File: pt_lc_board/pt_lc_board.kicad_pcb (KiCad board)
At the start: 2 copper layers, 152.4 x 140 mm, 29 parts, among them J1 DSUB1, J2 DSUB2, J3 DSUB3, J4 PCIE Socket, U1 HX711_Breakout, U10 PCF8575_Breakout, U2 HX711_Breakout, U3 HX711_Breakout, U5 HX711_Breakout, U6 HX711_Breakout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

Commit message: Mostly finished with board.
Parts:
- removed U10: PCF8575_Breakout, PCF8575_Breakout:PCF8575_Breakout
- added R10: 4.7k, Resistor_SMD:R_0603_1608Metric, F.Cu at (132.9, 136.3)
- added R11: 4.7k, Resistor_SMD:R_0603_1608Metric, F.Cu at (132.9, 131.0)
- added R9: 4.7k, Resistor_SMD:R_0603_1608Metric, F.Cu at (137.2, 133.6)
- added U7: PCF8575_Breakout, PCF8575_Breakout:PCF8575_Breakout, F.Cu at (64.2, 130.6)
- J4: value PCIE Socket -> PCIE Card Edge; footprint PCIE-LP-01-01-F-DV-A-TR:SAMTEC_PCIE-LP-01-01-F-DV-A-TR -> Connector_PCBEdge:BUS_PCIexpress_x1
- R1, R13, R17: footprint Resistor_SMD:R_1206_3216Metric -> Resistor_SMD:R_0603_1608Metric
- R12: renamed from R5; footprint Resistor_SMD:R_1206_3216Metric -> Resistor_SMD:R_0603_1608Metric
- R14: renamed from R6; footprint Resistor_SMD:R_1206_3216Metric -> Resistor_SMD:R_0603_1608Metric
- R15: renamed from R14; footprint Resistor_SMD:R_1206_3216Metric -> Resistor_SMD:R_0603_1608Metric
- R16: renamed from R15; footprint Resistor_SMD:R_1206_3216Metric -> Resistor_SMD:R_0603_1608Metric
- R18: renamed from R16; footprint Resistor_SMD:R_1206_3216Metric -> Resistor_SMD:R_0603_1608Metric
- R19: renamed from R18; footprint Resistor_SMD:R_1206_3216Metric -> Resistor_SMD:R_0603_1608Metric
- R2: renamed from R9; footprint Resistor_SMD:R_1206_3216Metric -> Resistor_SMD:R_0603_1608Metric
- R3: renamed from R2; footprint Resistor_SMD:R_1206_3216Metric -> Resistor_SMD:R_0603_1608Metric
- R4: renamed from R10; footprint Resistor_SMD:R_1206_3216Metric -> Resistor_SMD:R_0603_1608Metric
- R5: renamed from R3; footprint Resistor_SMD:R_1206_3216Metric -> Resistor_SMD:R_0603_1608Metric
- R6: renamed from R11; footprint Resistor_SMD:R_1206_3216Metric -> Resistor_SMD:R_0603_1608Metric
- R7: renamed from R4; footprint Resistor_SMD:R_1206_3216Metric -> Resistor_SMD:R_0603_1608Metric
- R8: renamed from R12; footprint Resistor_SMD:R_1206_3216Metric -> Resistor_SMD:R_0603_1608Metric
- moved J4 11.2 mm to (125.0, 144.9)
- moved J3 0.36 mm to (66.9, 10.6)
- moved J1 0.25 mm to (13.6, 10.6)
- moved R7 0.15 mm to (11.9, 93.1)
- moved R18 0.13 mm to (62.8, 19.4)
- moved R14 0.10 mm to (114.0, 55.3)
- moved J2 0.09 mm to (117.8, 10.6)
- renumbered U5 to U2, U2 to U3, U6 to U4, U3 to U5, U7 to U6
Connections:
- J4 pad B11: unconnected-(J4-PadB11) -> /Board_ID
- J4 pad B12: unconnected-(J4-PadB12) -> +5V
- J4 pad B13: unconnected-(J4-PadB13) -> +5V
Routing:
- net /IO_EXP_SCL: track 0.00 -> 62.4 mm, vias 0 -> 1
- net /IO_EXP_SDA: track 0.00 -> 62.1 mm, vias 0 -> 1
- net /Board_ID: track 0.00 -> 17.5 mm
- net +5V: track 0.00 -> 12.4 mm
- net /LC1_E+: track 17.4 -> 20.5 mm
- net /LC2_E+: track 56.6 -> 58.9 mm
- net GND: track 0.00 -> 2.00 mm
- net /PT6_E+: track 95.4 -> 97.3 mm
- net /PT4_E+: track 17.0 -> 18.9 mm
- net /PT5_E+: track 55.1 -> 56.9 mm
- net /PT1_E+: track 16.8 -> 18.5 mm
- net /PT2_E+: track 56.2 -> 57.9 mm
- net /PT3_E+: track 95.0 -> 96.5 mm
- net +3V3: track 442.7 -> 443.7 mm
- net Net-(R1-Pad2): track 7.27 -> 8.24 mm
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- added copper zone on B.Cu, net GND
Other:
- outline, holes or cut-outs redrawn
- board text added: "DNE PT board 2 only!"

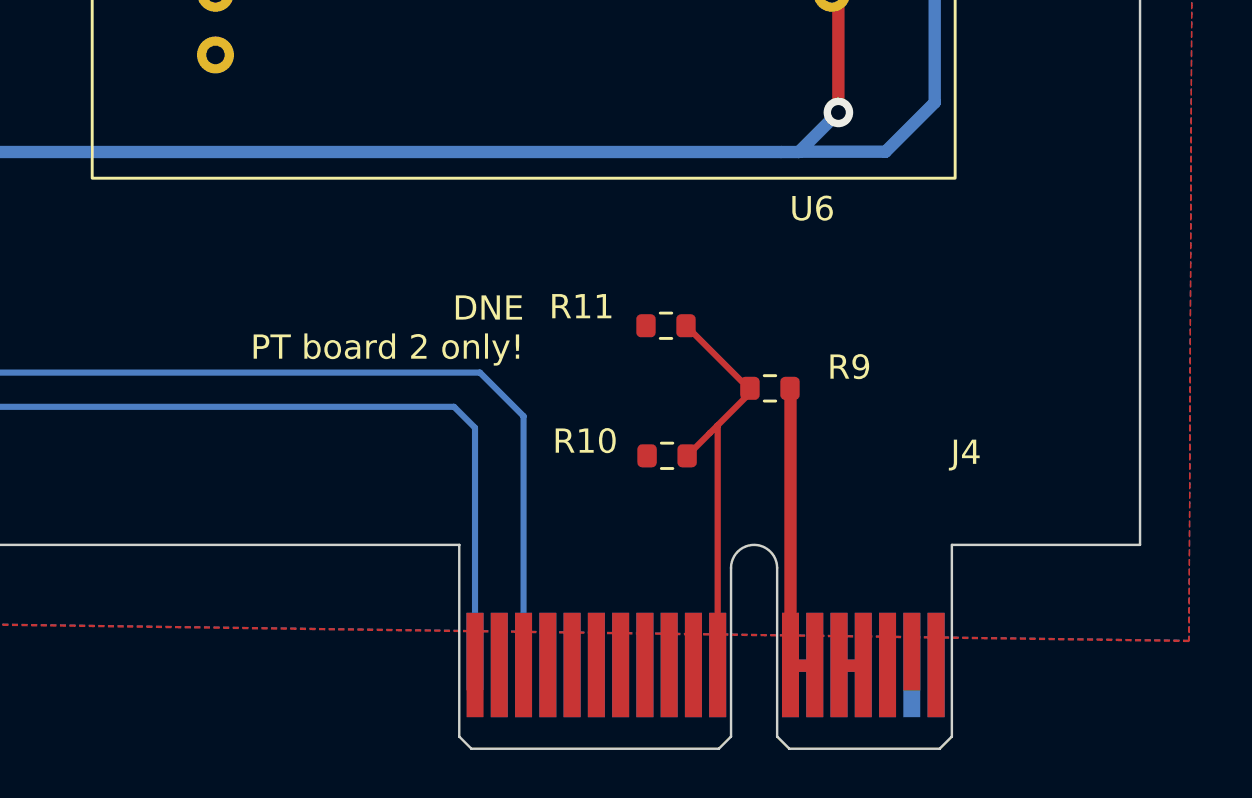
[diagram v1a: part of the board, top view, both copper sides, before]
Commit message: Updated board_ID.
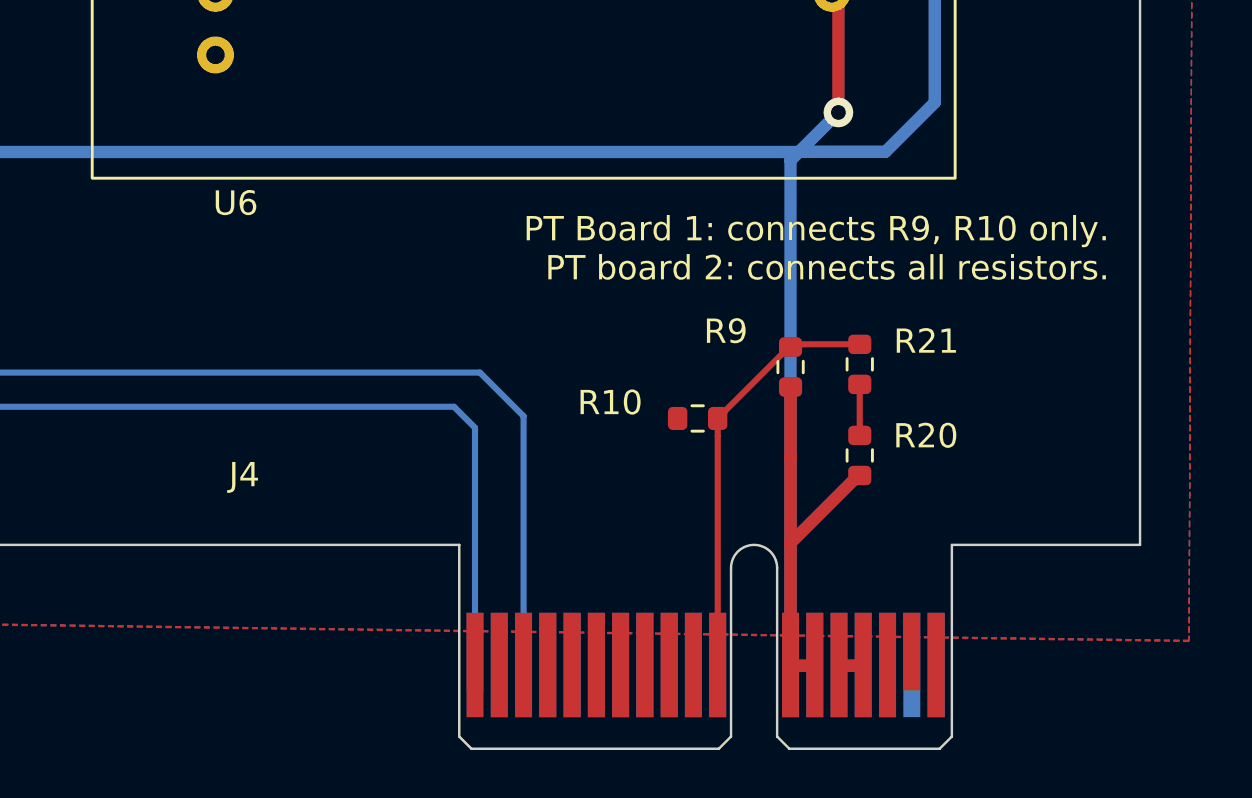
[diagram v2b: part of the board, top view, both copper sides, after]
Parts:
- removed R11: 4.7k, Resistor_SMD:R_0603_1608Metric
- added R20: 4.7k, Resistor_SMD:R_0603_1608Metric, F.Cu at (140.8, 136.3)
- added R21: 4.7k, Resistor_SMD:R_0603_1608Metric, F.Cu at (140.8, 132.6)
- moved R10 1.99 mm to (134.2, 134.8)
- moved R9 1.22 mm to (138.0, 132.7), turned to -90 degrees
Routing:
- net +3V3: track 443.7 -> 465.0 mm
- net +5V: track 12.4 -> 16.5 mm
- net Net-(R20-Pad1): track 0.00 -> 2.11 mm
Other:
- board text added: "PT Board 1: connects R9, R10 only. PT board 2: connects all resistors."
- board text removed: "DNE PT board 2 only!"
